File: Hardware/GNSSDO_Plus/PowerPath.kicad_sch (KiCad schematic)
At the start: 44 parts, among them Q2 DMG2305UX, Q3 DMG2305UX, Q4 DMG2305UX, Q5 DMG2305UX, Q6 DMG2305UX, Q7 DMG2305UX, Q8 DMG2305UX, Q9 DMG2305UX, U26 LTC4418, U27 LTC4418

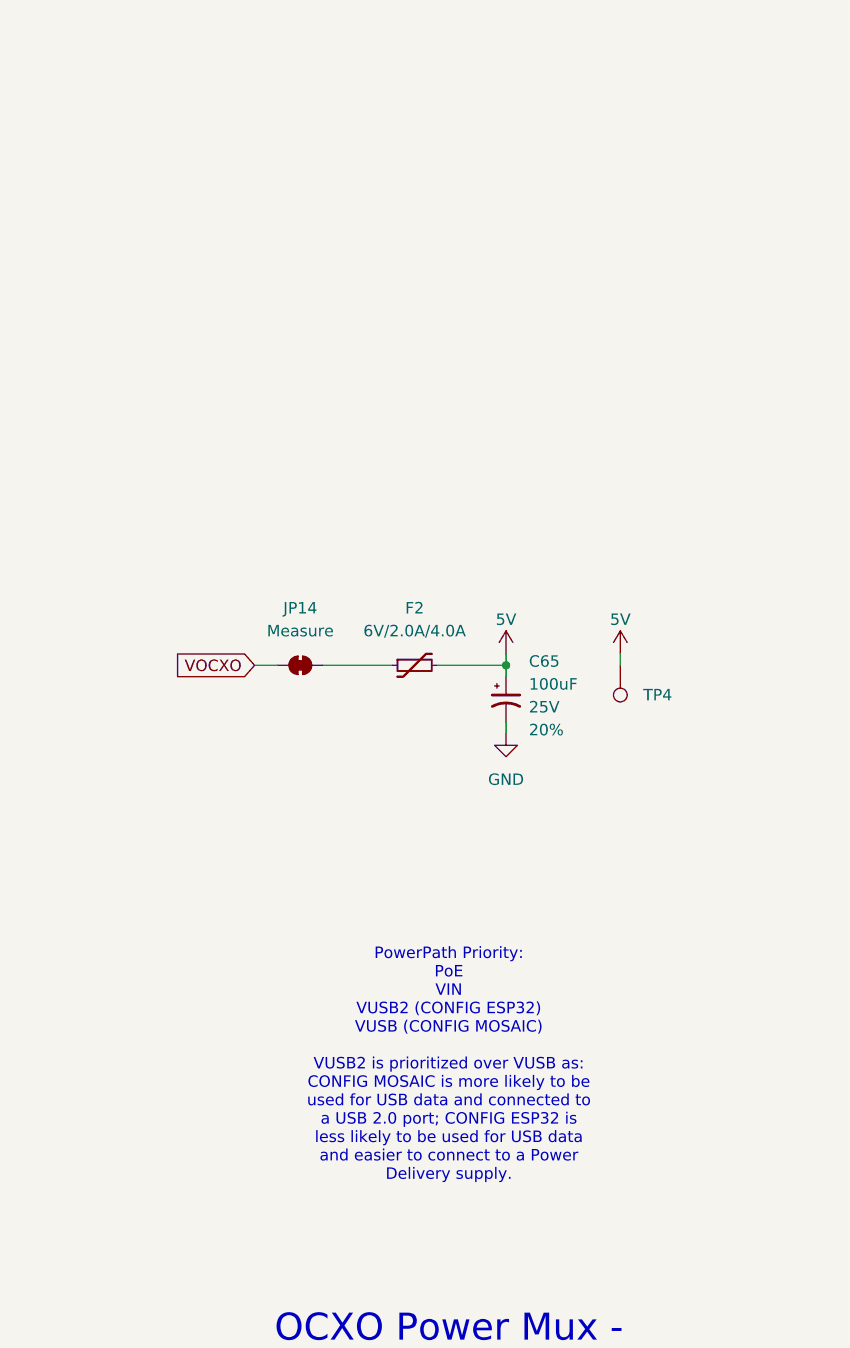
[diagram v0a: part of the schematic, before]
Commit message: Update GNSSDO KiCad files to match latest SparkFun library
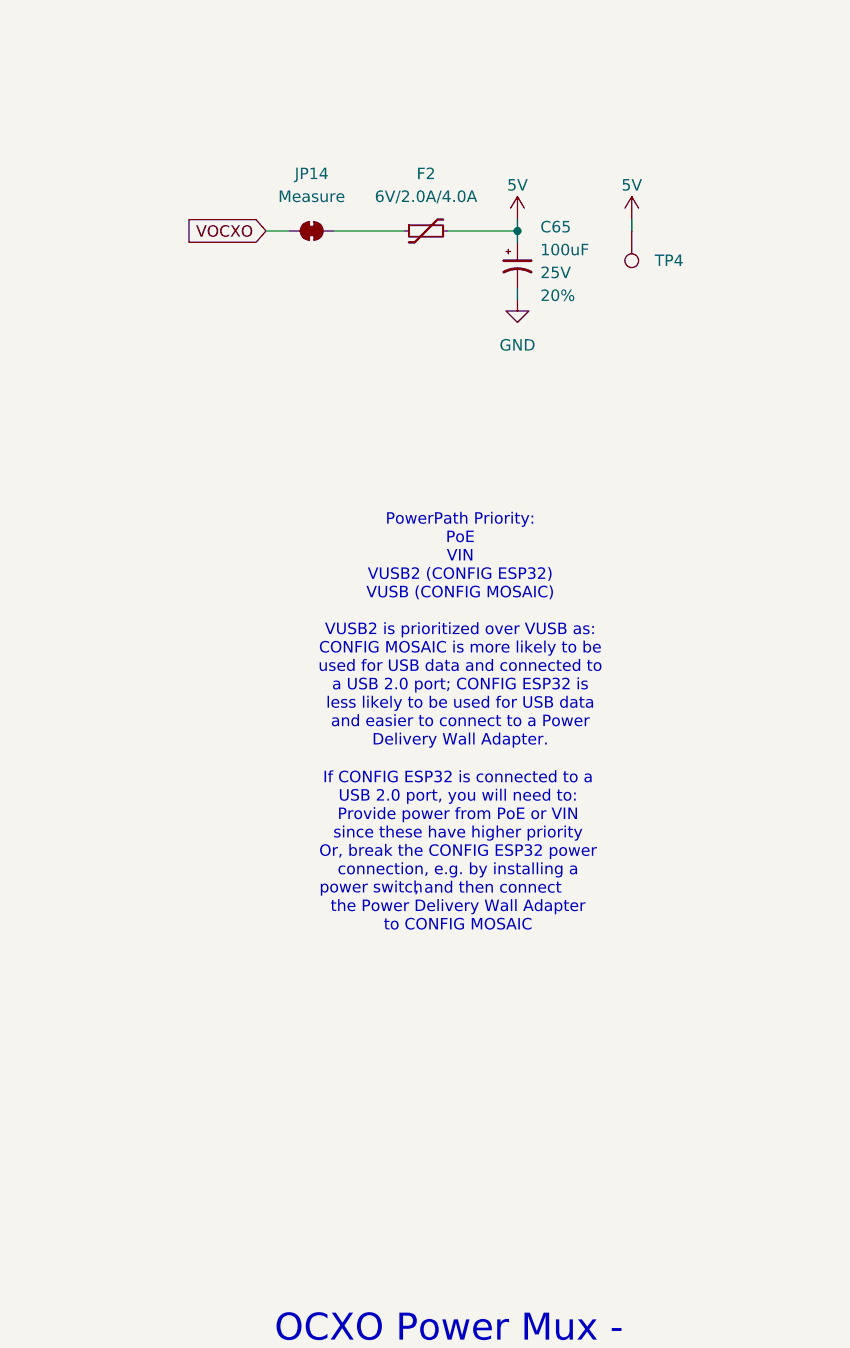
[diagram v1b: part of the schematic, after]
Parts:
- TP4: footprint SparkFun-Connector:1x01 -> SparkFun-Connector:1x01_P2.54mm
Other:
- note added: "If CONFIG ESP32 is connected to a USB 2.0 port, you will need to: Provide power from PoE or VIN since these have higher priority Or, break the CONFIG ESP32 power connection, e.g. by installing a , and then connect the Power Delivery Wall Adapter to CONFIG MOSAIC"
- note added: "PowerPath Priority: PoE VIN VUSB2 (CONFIG ESP32) VUSB (CONFIG MOSAIC) VUSB2 is prioritized over VUSB as: CONFIG MOSAIC is more likely to be used for USB data and connected to a USB 2.0 port; CONFIG ESP32 is less likely to be used for USB data and easier to connect to a Power Delivery Wall Adapter."
- note added: "power switch"
- note removed: "PowerPath Priority: PoE VIN VUSB2 (CONFIG ESP32) VUSB (CONFIG MOSAIC) VUSB2 is prioritized over VUSB as: CONFIG MOSAIC is more likely to be used for USB data and connected to a USB 2.0 port; CONFIG ESP32 is less likely to be used for USB data and easier to connect to a Power Delivery supply."
- moved on the sheet: C65, F2, JP14, TP4
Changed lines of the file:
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@@
 		)
 	)
-	(text "PowerPath Priority:\nPoE\nVIN\nVUSB2 (CONFIG ESP32)\nVUSB (CONFIG MOSAIC)\n\nVUSB2 is prioritized over VUSB as:\nCONFIG MOSAIC is more likely to be\nused for USB data and connected to\na USB 2.0 port; CONFIG ESP32 is\nless likely to be used for USB data\nand easier to connect to a Power\nDelivery supply."
+	(text "If CONFIG ESP32 is connected to a\nUSB 2.0 port, you will need to:\nProvide power from PoE or VIN\nsince these have higher priority\nOr, break the CONFIG ESP32 power\nconnection, e.g. by installing a\n            , and then connect\nthe Power Delivery Wall Adapter\nto CONFIG MOSAIC"
 		(exclude_from_sim no)
-		(at 228.6 142.24 0)
+		(at 229.616 118.618 0)
+		(effects
+			(font
+				(size 1.27 1.27)
+				(color 132 132 132 1)
+			)
+		)
+	)
+	(text "power switch"
+		(exclude_from_sim no)
+		(at 219.964 122.682 0)
+		(effects
+			(font
+				(size 1.27 1.27)
+				(color 132 132 132 1)
+			)
+			(href "https://www.sparkfun.com/usb-c-extension-cable-with-power-switch-1m.html")
+		)
+	)
+	(text "PowerPath Priority:\nPoE\nVIN\nVUSB2 (CONFIG ESP32)\nVUSB (CONFIG MOSAIC)\n\nVUSB2 is prioritized over VUSB as:\nCONFIG MOSAIC is more likely to be\nused for USB data and connected to\na USB 2.0 port; CONFIG ESP32 is\nless likely to be used for USB data\nand easier to connect to a Power\nDelivery Wall Adapter."
+		(exclude_from_sim no)
+		(at 229.87 93.98 0)
 		(effects
 			(font
@@
 	)
 	(junction
-		(at 234.95 97.79)
+		(at 236.22 49.53)
 		(diameter 0)
 		(color 0 0 0 0)
@@
 	(wire
 		(pts
-			(xy 214.63 97.79) (xy 222.25 97.79)
+			(xy 215.9 49.53) (xy 223.52 49.53)
 		)
 		(stroke
@@
 	(wire
 		(pts
-			(xy 234.95 96.52) (xy 234.95 97.79)
+			(xy 236.22 48.26) (xy 236.22 49.53)
 		)
 		(stroke
@@
 	(wire
 		(pts
-			(xy 247.65 96.52) (xy 247.65 97.79)
+			(xy 248.92 48.26) (xy 248.92 49.53)
 		)
 		(stroke
@@
 	(wire
 		(pts
-			(xy 227.33 97.79) (xy 234.95 97.79)
+			(xy 228.6 49.53) (xy 236.22 49.53)
 		)
 		(stroke
@@
 	(wire
 		(pts
-			(xy 234.95 104.14) (xy 234.95 105.41)
+			(xy 236.22 55.88) (xy 236.22 57.15)
 		)
 		(stroke
@@
 	(wire
 		(pts
-			(xy 207.01 97.79) (xy 209.55 97.79)
+			(xy 208.28 49.53) (xy 210.82 49.53)
 		)
 		(stroke
@@
 	(wire
 		(pts
-			(xy 234.95 97.79) (xy 234.95 99.06)
+			(xy 236.22 49.53) (xy 236.22 50.8)
 		)
 		(stroke
@@
 	(global_label "VOCXO"
 		(shape input)
-		(at 207.01 97.79 180)
+		(at 208.28 49.53 180)
 		(fields_autoplaced yes)
 		(effects
@@
 		)
 		(property "Intersheetrefs" "${INTERSHEET_REFS}"
-			(at 197.7957 97.79 0)
+			(at 199.0657 49.53 0)
 			(effects
 				(font
@@
 	(symbol
 		(lib_id "power:GND")
-		(at 234.95 105.41 0)
+		(at 236.22 57.15 0)
 		(unit 1)
 		(exclude_from_sim no)
@@
 		(fields_autoplaced yes)
 		(property "Reference" "#PWR231"
-			(at 234.95 111.76 0)
+			(at 236.22 63.5 0)
 			(effects
 				(font
@@
 		)
 		(property "Value" "GND"
-			(at 234.95 110.49 0)
+			(at 236.22 62.23 0)
 			(effects
 				(font
@@
 		)
 		(property "Footprint" ""
-			(at 234.95 105.41 0)
+			(at 236.22 57.15 0)
 			(effects
 				(font
@@
 		)
 		(property "Datasheet" ""
-			(at 234.95 105.41 0)
+			(at 236.22 57.15 0)
 			(effects
 				(font
@@
 		)
 		(property "Description" "Power symbol creates a global label with name \"GND\" , ground"
-			(at 234.95 105.41 0)
+			(at 236.22 57.15 0)
 			(effects
 				(font
@@
 	(symbol
 		(lib_id "SparkFun-Connector:TestPoint_PTH")
-		(at 247.65 97.79 180)
+		(at 248.92 49.53 180)
 		(unit 1)
 		(exclude_from_sim no)
@@
 		(fields_autoplaced yes)
 		(property "Reference" "TP4"
-			(at 250.19 101.0919 0)
+			(at 251.46 52.8319 0)
 			(effects
 				(font
@@
 		)
 		(property "Value" "PTH"
-			(at 247.65 93.98 0)
+			(at 248.92 45.72 0)
 			(effects
 				(font
@@
 			)
 		)
-		(property "Footprint" "SparkFun-Connector:1x01"
-			(at 248.92 91.44 0)
+		(property "Footprint" "SparkFun-Connector:1x01_P2.54mm"
+			(at 250.19 43.18 0)
 			(effects
 				(font
@@
 		)
 		(property "Datasheet" "~"
-			(at 247.65 90.17 0)
+			(at 248.92 41.91 0)
 			(effects
 				(font
@@
 		)
 		(property "Description" "Test Point"
-			(at 247.65 87.63 0)
+			(at 248.92 39.37 0)
 			(effects
 				(font
@@
 	(symbol
 		(lib_id "SparkFun-Capacitor:100uF_6.6x6.6_25V_20%")
-		(at 234.95 101.6 0)
+		(at 236.22 53.34 0)
 		(unit 1)
 		(exclude_from_sim no)
@@
 		(fields_autoplaced yes)
 		(property "Reference" "C65"
-			(at 237.49 97.3581 0)
+			(at 238.76 49.0981 0)
 			(effects
 				(font
@@
 		)
 		(property "Value" "100uF"
-			(at 237.49 99.8981 0)
+			(at 238.76 51.6381 0)
 			(effects
 				(font
@@
 		)
 		(property "Footprint" "SparkFun-Capacitor:Panasonic_D"
-			(at 234.95 119.38 0)
+			(at 236.22 71.12 0)
 			(effects
 				(font
@@
 		)
 		(property "Datasheet" "https://www.chemi-con.co.jp/products/relatedfiles/capacitor/catalog/MVARA-e.PDF"
-			(at 236.22 116.84 0)
+			(at 237.49 68.58 0)
 			(effects
 				(font
@@
 		)
 		(property "Description" "Polarized capacitor, US symbol, 0.248\" Dia x 0.303\" H, Electrolitic"
-			(at 235.458 122.174 0)
+			(at 236.728 73.914 0)
 			(effects
 				(font
@@
 		)
 		(property "PROD_ID" "CAP-12547"
-			(at 234.95 114.3 0)
+			(at 236.22 66.04 0)
 			(effects
 				(font
@@
 		)
 		(property "Voltage" "25V"
-			(at 237.49 102.4381 0)
+			(at 238.76 54.1781 0)
 			(effects
 				(font
@@
 		)
 		(property "Tolerance" "20%"
-			(at 237.49 104.9781 0)
+			(at 238.76 56.7181 0)
 			(effects
 				(font
@@
 	(symbol
 		(lib_id "SparkFun-Fuse:Fuse 6V/2.0A/4.0A")
-		(at 224.79 97.79 0)
+		(at 226.06 49.53 0)
 		(unit 1)
 		(exclude_from_sim no)
@@
 		(fields_autoplaced yes)
 		(property "Reference" "F2"
-			(at 224.79 91.44 0)
+			(at 226.06 43.18 0)
 			(effects
 				(font
@@
 		)
 		(property "Value" "6V/2.0A/4.0A"
-			(at 224.79 93.98 0)
+			(at 226.06 45.72 0)
 			(effects
 				(font
@@
 		)
 		(property "Footprint" "SparkFun-Fuse:1210"
-			(at 224.79 105.41 0)
+			(at 226.06 57.15 0)
 			(effects
 				(font
@@
 		)
 		(property "Datasheet" "https://www.belfuse.com/resources/datasheets/circuitprotection/ds-cp-0zch-series.pdf"
-			(at 225.806 103.378 0)
+			(at 227.076 55.118 0)
 			(effects
 				(font
@@
 		)
 		(property "Description" "Resettable fuse 2A"
-			(at 224.79 110.49 0)
+			(at 226.06 62.23 0)
 			(effects
 				(font
@@
 		)
 		(property "PROD_ID" "RES-14313"
-			(at 224.79 107.95 0)
+			(at 226.06 59.69 0)
 			(effects
 				(font
@@
 	(symbol
 		(lib_id "SparkFun-PowerSymbol:5V")
-		(at 234.95 96.52 0)
+		(at 236.22 48.26 0)
 		(unit 1)
 		(exclude_from_sim no)
@@
 		(fields_autoplaced yes)
 		(property "Reference" "#PWR42"
-			(at 234.95 100.33 0)
+			(at 236.22 52.07 0)
 			(effects
 				(font
@@
 		)
 		(property "Value" "5V"
-			(at 234.95 92.71 0)
+			(at 236.22 44.45 0)
 			(do_not_autoplace yes)
 			(effects
@@
 		)
 		(property "Footprint" ""
-			(at 234.95 96.52 0)
+			(at 236.22 48.26 0)
 			(effects
 				(font
@@
 		)
 		(property "Datasheet" ""
-			(at 234.95 96.52 0)
+			(at 236.22 48.26 0)
 			(effects
 				(font
@@
 		)
 		(property "Description" "Power symbol creates a global label with name \"5V\""
-			(at 234.95 102.87 0)
+			(at 236.22 54.61 0)
 			(effects
 				(font
@@
 	(symbol
 		(lib_id "SparkFun-Jumper:Jumper_Measure")
-		(at 212.09 97.79 0)
+		(at 213.36 49.53 0)
 		(unit 1)
 		(exclude_from_sim no)
@@
 		(fields_autoplaced yes)
 		(property "Reference" "JP14"
-			(at 212.09 91.44 0)
+			(at 213.36 43.18 0)
 			(effects
 				(font
@@
 		)
 		(property "Value" "Measure"
-			(at 212.09 93.98 0)
+			(at 213.36 45.72 0)
 			(effects
 				(font
@@
 		)
 		(property "Footprint" "SparkFun-Jumper:Jumper_2_PTH_SMD_Combo-NC"
-			(at 211.836 102.362 0)
+			(at 213.106 54.102 0)
 			(effects
 				(font
@@
 		)
 		(property "Datasheet" "~"
-			(at 212.09 105.41 0)
+			(at 213.36 57.15 0)
 			(effects
 				(font
@@
 		)
 		(property "Description" "Solder Jumper, 2-pole, closed/bridged"
-			(at 212.09 107.95 0)
+			(at 213.36 59.69 0)
 			(effects
 				(font
@@
 	(symbol
 		(lib_id "SparkFun-PowerSymbol:5V")
-		(at 247.65 96.52 0)
+		(at 248.92 48.26 0)
 		(unit 1)
 		(exclude_from_sim no)
@@
 		(fields_autoplaced yes)
 		(property "Reference" "#PWR30"
-			(at 247.65 100.33 0)
+			(at 248.92 52.07 0)
 			(effects
 				(font
@@
 		)
 		(property "Value" "5V"
-			(at 247.65 92.71 0)
+			(at 248.92 44.45 0)
 			(do_not_autoplace yes)
 			(effects
@@
 		)
 		(property "Footprint" ""
-			(at 247.65 96.52 0)
+			(at 248.92 48.26 0)
 			(effects
 				(font
@@
 		)
 		(property "Datasheet" ""
-			(at 247.65 96.52 0)
+			(at 248.92 48.26 0)
 			(effects
 				(font
@@
 		)
 		(property "Description" "Power symbol creates a global label with name \"5V\""
-			(at 247.65 102.87 0)
+			(at 248.92 54.61 0)
 			(effects
 				(font
